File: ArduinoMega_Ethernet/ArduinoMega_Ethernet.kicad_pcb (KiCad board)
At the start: 2 copper layers, 101.6 x 53.3 mm, 114 parts, among them J1 RJ45_Amphenol_RJMG1BD3B8K1ANR, J11 Micro_SD_Card_Det_Hirose_DM3AT, J2 SD_DET_JUMP, J3 IMU_INT1_JUMP, J4 IMU_INT2_JUMP, J5 ETHER_INT_JUMP, J6 RTC_MFP_JUMP, J7 EXT_3V3_I2C, J9 PROGRAM_POWER_USBC, SW1 RST_BTN, U1 ATmega2560-16A, U10 TXS0108EPW, U2 CH340C, U3 ISM330DHCX, U4 W5500, U6 AP63203WU, U7 SE050C2HQ1, U8 AP22804AW5, U9 MCP7940N-xST, Y1 16Mhz, Y2 25Mhz, Y3 32.768kHz

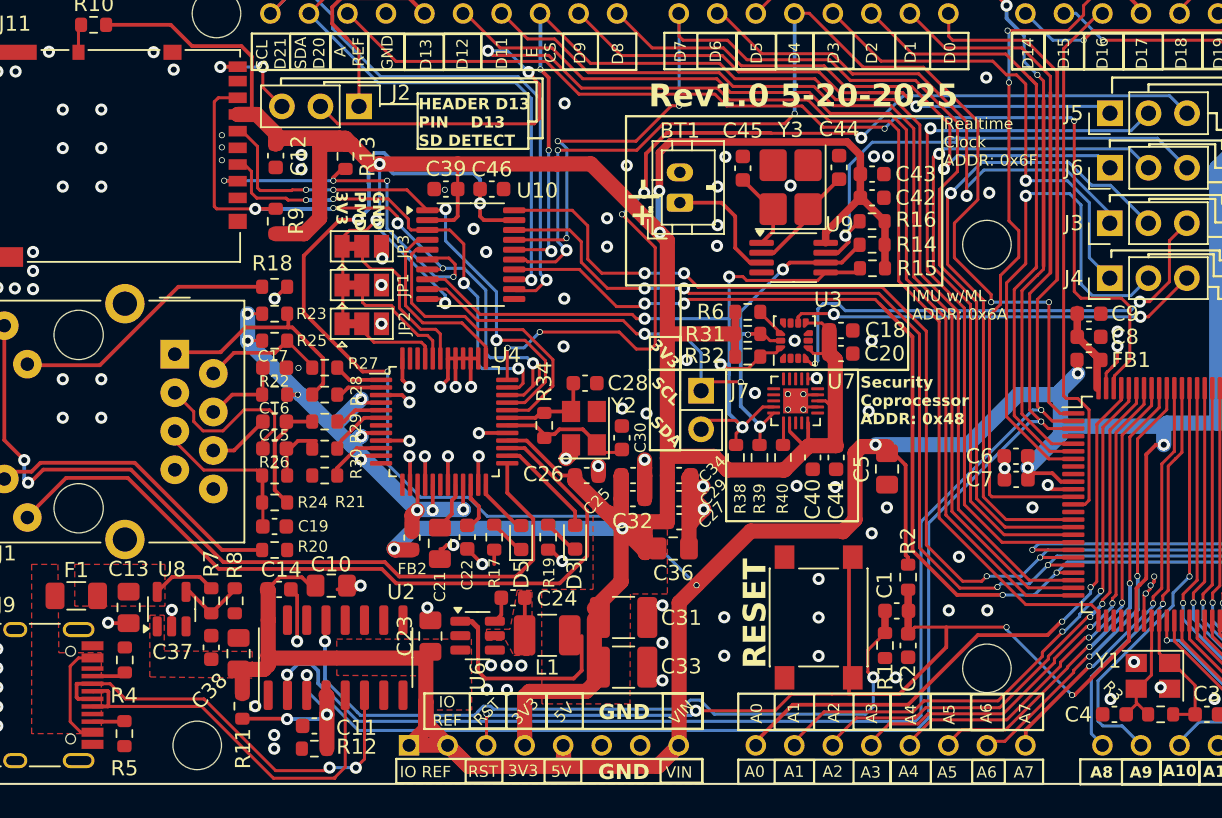
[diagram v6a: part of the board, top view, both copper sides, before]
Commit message: fix VIN pin
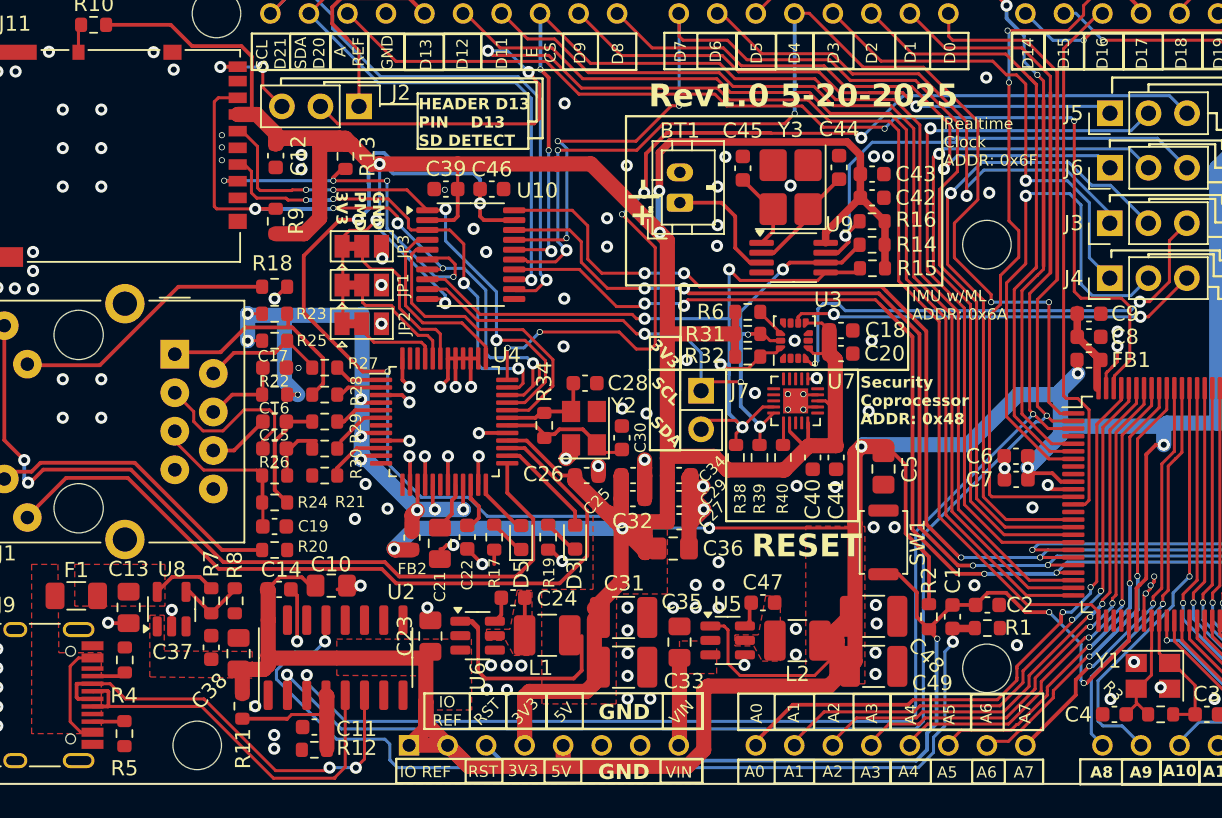
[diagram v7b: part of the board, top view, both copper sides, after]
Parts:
- added C35: 10uF, Capacitor_SMD:C_0805_2012Metric_Pad1.18x1.45mm_HandSolder, F.Cu at (88.9, 172.3)
- added C47: 100nF, Capacitor_SMD:C_0603_1608Metric, F.Cu at (94.4, 169.7)
- added C48: 22uF, Capacitor_SMD:C_1210_3225Metric_Pad1.33x2.70mm_HandSolder, F.Cu at (101.7, 170.6)
- added C49: 22uF, Capacitor_SMD:C_1210_3225Metric_Pad1.33x2.70mm_HandSolder, F.Cu at (101.7, 173.9)
- added L2: 4.7uH, Inductor_SMD:L_1210_3225Metric_Pad1.42x2.65mm_HandSolder, F.Cu at (96.7, 172.2)
- added U5: AP63205WU, Package_TO_SOT_SMD:TSOT-23-6, F.Cu at (92.1, 172.2)
- L1: value 4.7uH -> 3.9uH
- SW1: value RST_BTN -> SW_Push; footprint Button_Switch_SMD:SW_SPST_PTS645 -> Button_Switch_SMD:SW_Push_SPST_NO_Alps_SKRK
- moved R1 6.85 mm to (109.2, 171.3), turned to 0 degrees
- moved SW1 6.54 mm to (102.4, 165.7), turned to -90 degrees
- moved C2 5.87 mm to (109.2, 169.8), turned to 180 degrees
- moved C1 3.69 mm to (106.9, 170.6), turned to 90 degrees
- moved R2 2.95 mm to (105.4, 170.6)
- moved C5 0.23 mm to (102.4, 160.9)
- moved C11 0.07 mm to (64.8, 177.9)
- moved R12 0.07 mm to (64.8, 179.4)
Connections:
- A1 pad VIN: +5V -> VIN+
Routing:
- net +5V: track 272.0 -> 303.5 mm
- net /PWRandPRG/PROGRAM_~{DTR}: track 49.2 -> 62.9 mm
- net Net-(FB2-Pad2): track 40.7 -> 50.5 mm
- net VIN+: track 0.00 -> 5.79 mm
- net /MCU_RESET: track 67.2 -> 64.3 mm, vias 4 -> 3
- net +3V3: track 271.9 -> 269.2 mm
- net /PIN_D1: track 105.5 -> 103.2 mm
- net /PIN_D51: track 91.5 -> 89.5 mm
- net /PIN_D50: track 90.3 -> 88.5 mm
- net /PIN_D52: track 85.5 -> 83.8 mm
- net Net-(U5-BST): track 0.00 -> 1.69 mm
- net /PIN_A0: track 40.5 -> 42.0 mm
- net /PIN_D0: track 104.6 -> 103.7 mm
- net /PWRandPRG/IMU_SDA: track 53.3 -> 54.0 mm
- net Net-(U2-V3): vias 2 -> 0
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- added copper zone on F.Cu, net Net-(U5-SW)
- added copper zone on F.Cu, net VIN+

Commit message: finished BOM and component sizing
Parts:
- C1: value TBD -> 100nF
- C2: value TBD -> 22pF
- C28, C30: value Var -> 18pF; footprint Capacitor_SMD:C_0603_1608Metric -> Capacitor_SMD:C_0402_1005Metric_Pad0.74x0.62mm_HandSolder
- C44, C45: value TBD -> 12pF; footprint Capacitor_SMD:C_0603_1608Metric -> Capacitor_SMD:C_0402_1005Metric_Pad0.74x0.62mm_HandSolder
- L1, L2: footprint Inductor_SMD:L_1210_3225Metric_Pad1.42x2.65mm_HandSolder -> Inductor_SMD:L_APV_ANR6028
- Y3: footprint Crystal:Crystal_SMD_3225-4Pin_3.2x2.5mm_HandSoldering -> Crystal:Crystal_SMD_EuroQuartz_EQ161-2Pin_3.2x1.5mm_HandSoldering
- moved C1 89.0 mm to (168.0, 105.9)
- moved C2 89.0 mm to (170.3, 105.1), turned to 0 degrees
- moved R1 89.0 mm to (170.3, 106.6)
- moved R2 89.0 mm to (166.5, 105.9)
- moved C31 89.0 mm to (146.2, 105.8)
- moved C33 89.0 mm to (146.2, 109.1)
- moved C48 88.6 mm to (162.3, 105.9)
- moved C49 88.6 mm to (162.3, 109.2)
- moved L1 88.0 mm to (140.3, 107.5)
- moved L2 88.0 mm to (156.3, 107.5)
- moved C23 87.9 mm to (134.8, 109.9), turned to 0 degrees
- moved C45 87.9 mm to (153.6, 77.3), turned to 0 degrees
- moved SW1 87.8 mm to (161.6, 100.8)
- moved A1 87.7 mm to (153.1, 90.2)
- moved BT1 87.7 mm to (148.1, 78.5)
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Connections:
- Y3 pad 2: GND -> Net-(U9-X1)
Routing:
- net +5V: track 303.5 -> 282.3 mm
- net Net-(U6-SW): track 2.48 -> 7.11 mm
- net VIN+: track 5.79 -> 10.1 mm
- net /PIN_D22: track 29.5 -> 26.1 mm
- net GND: track 70.6 -> 68.7 mm, vias 153 -> 150
- net +3V3: track 269.2 -> 271.1 mm
- net Net-(U9-X1): track 5.34 -> 6.66 mm
- net /PIN_D24: track 24.6 -> 23.4 mm
- net /MCU_RESET: track 64.3 -> 65.4 mm
- net /PWRandPRG/PROGRAM_~{DTR}: track 62.9 -> 63.9 mm
- net /PIN_D23: track 28.7 -> 27.8 mm
- net /PIN_D38: track 47.8 -> 47.1 mm
- net /PIN_D52: track 83.8 -> 83.3 mm
- removed copper zone on F.Cu, net VIN+
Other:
- board text added: "Rev1.0 5-22-2025"
- board text removed: "Rev1.0 5-20-2025"
